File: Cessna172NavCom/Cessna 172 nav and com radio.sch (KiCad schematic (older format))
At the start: 21 parts, among them J1 Conn_02x10_Odd_Even, J2 USB_B_Micro, J6 Conn_01x05, SW1 SW_Push, SW2 SW_Push, SW3 SW_Push

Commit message: Mostly laid out
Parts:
- removed J1: Conn_02x10_Odd_Even, Connector_PinHeader_2.54mm:PinHeader_2x10_P2.54mm_Vertical, symbol Connector_Generic:Conn_02x10_Odd_Even
- removed J6: Conn_01x05, Connector_PinHeader_2.54mm:PinHeader_1x05_P2.54mm_Vertical, symbol Connector_Generic:Conn_01x05
- added C12, C13, C14, C15: 0.1uF, Capacitor_SMD:C_0805_2012Metric_Pad1.15x1.40mm_HandSolder, symbol Device:C
- added D5, D6, D7: LED, LED_THT:LED_D5.0mm, symbol Device:LED
- added J8: Conn_02x20_Odd_Even, SamacSys_Parts:SAMTEC-TST-120-01-X-D, symbol Connector_Generic:Conn_02x20_Odd_Even
- added R18, R19, R20: 220k, Resistor_SMD:R_0805_2012Metric_Pad1.15x1.40mm_HandSolder, symbol Device:R
- added SW4, SW5, SW6: SW_Push, Button_Switch_THT:SW_PUSH_6mm_H8mm, symbol Switch:SW_Push
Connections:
- net labels added: CHAN1_LED, CHAN2_LED, COMM1_KHZ_SW, COMM1_LEFT, COMM1_RIGHT, COMM1_TX_SW, COMM1_VOL_LEFT, COMM1_VOL_RIGHT, COMM2_KHZ_SW, COMM2_LEFT, COMM2_RIGHT, COMM2_TX_SW, COMM2_VOL_LEFT, COMM2_VOL_RIGHT, IDENT1_LED, IDENT1_SW, IDENT2_LED, IDENT2_SW, NAV1_KHZ_SW, NAV1_LEFT, NAV1_RIGHT, NAV1_TX_SW, NAV2_KHZ_SW, NAV2_LEFT, NAV2_RIGHT, NAV2_TX_SW, TEST1_LED, TEST1_SW, TEST2_LED, TEST2_SW
- net labels removed: CHAN_LED, COMM_KHZ_SW, COMM_LEFT, COMM_RIGHT, COMM_TX_SW, COMM_VOL_LEFT, COMM_VOL_RIGHT, DOUT, IDENT_LED, IDENT_SW, NAV_KHZ_SW, NAV_LEFT, NAV_RIGHT, NAV_TX_SW, TEST_LED, TEST_SW
- wire segments 44 -> 86
- no-connect marks 5 -> 6
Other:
- note added: "Arduino connections"
- note added: "COMM1 active"
- note added: "COMM1 standby"
- note added: "COMM1 tuning"
- note added: "COMM1 volume"
- note added: "COMM2 active"
- note added: "COMM2 standby"
- note added: "COMM2 tuning"
- note added: "COMM2 volume"
- note added: "Decoupling capacitors"
- note added: "NAV1 active"
- note added: "NAV1 standby"
- note added: "NAV1 tuning"
- note added: "NAV2 active"
- note added: "NAV2 standby"
- note added: "NAV2 tuning"
- note added: "Power"
- note added: "Test switch is on\nCOMM1 volume\nrotary encoder"
- note added: "Test switch is on\nCOMM2 volume\nrotary encoder"
- note removed: "COMM"
- note removed: "COMM active"
- note removed: "COMM standby"
- note removed: "COMM volume"
- note removed: "NAV"
- note removed: "NAV active"
- note removed: "NAV standby"
- note removed: "Power and board connection"
- note removed: "Test switch is on\nCOMM volume\nrotary encoder"
- moved on the sheet: C1, C2, C3, C4, C5, D1, D2, D3, D4, J2, R1, R17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

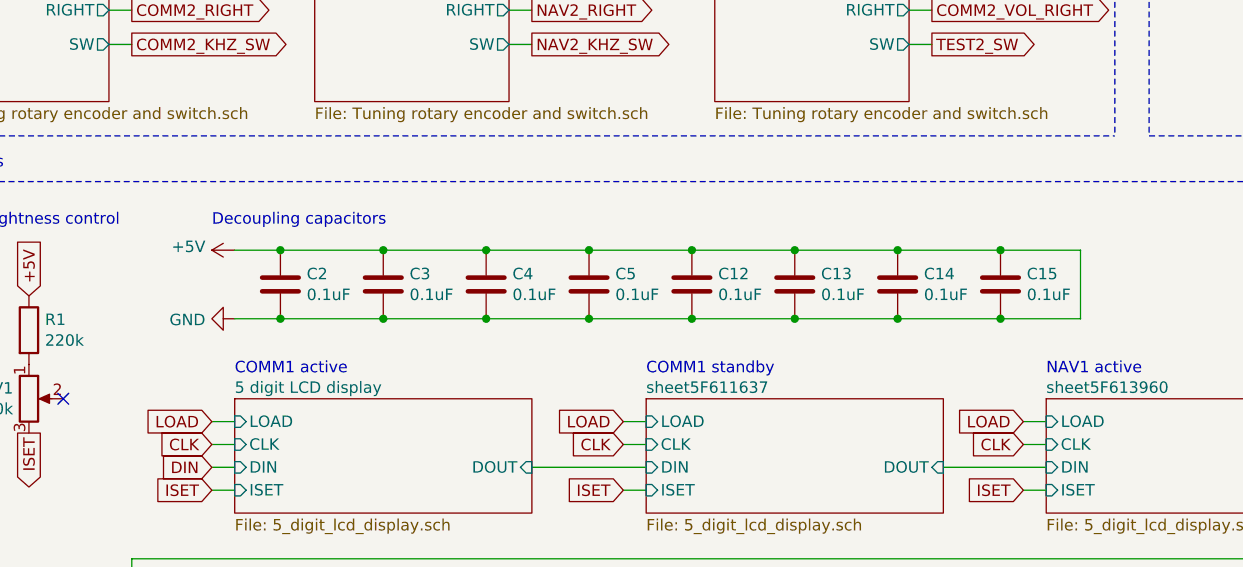
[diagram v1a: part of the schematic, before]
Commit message: Full 2up layout done
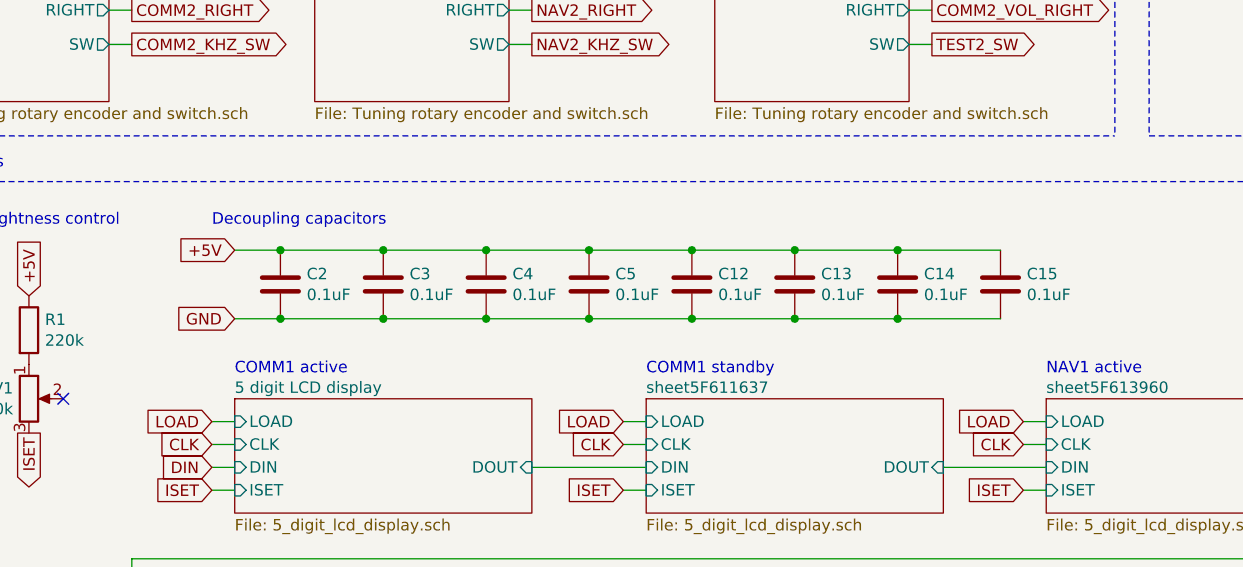
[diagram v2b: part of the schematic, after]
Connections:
- net +5V: no longer C1.2, C12.2, C13.2, C14.2, C15.2, C2.2, C3.2, C4.2, C5.2, D1.1 (K), D2.1 (K), D3.1 (K), D4.1 (K), D5.1 (K), D6.1 (K), D7.1 (K), J2.5 (GND), SW1.1, SW2.1, SW3.1, SW4.1, SW5.1, SW6.1
- new net GND: C1.2, C12.2, C13.2, C14.2, C15.2, C2.2, C3.2, C4.2, C5.2, D1.1 (K), D2.1 (K), D3.1 (K), D4.1 (K), D5.1 (K), D6.1 (K), D7.1 (K), J2.5 (GND), SW1.1, SW2.1, SW3.1, SW4.1, SW5.1, SW6.1
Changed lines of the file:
@@
 	4300 7100 4350 7100
-$Comp
-L power:+5V #PWR0101
-U 1 1 5F65C5FC
-P 2050 3500
-F 0 "#PWR0101" H 2050 3350 50  0001 C CNN
-F 1 "+5V" V 2065 3628 50  0000 L CNN
-F 2 "" H 2050 3500 50  0001 C CNN
-F 3 "" H 2050 3500 50  0001 C CNN
-	1    2050 3500
-	0    -1   -1   0
-$EndComp
-$Comp
-L power:GND #PWR0102
-U 1 1 5F65CDCA
-P 2050 3800
-F 0 "#PWR0102" H 2050 3550 50  0001 C CNN
-F 1 "GND" V 2055 3672 50  0000 R CNN
-F 2 "" H 2050 3800 50  0001 C CNN
-F 3 "" H 2050 3800 50  0001 C CNN
-	1    2050 3800
-	0    1    1    0
-$EndComp
 $Comp
 L Device:C C12
@@
 	1    0    0    -1
 $EndComp
-Connection ~ 5400 3500
-Connection ~ 5400 3800
 $Comp
 L Device:C C13
@@
 	4950 3800 5400 3800
 Connection ~ 4950 3800
-Wire Wire Line
-	5750 3500 5750 3800
-Wire Wire Line
-	5400 3800 5750 3800
-Wire Wire Line
-	5400 3500 5750 3500
 Wire Wire Line
 	3600 3500 4050 3500
@@
 Text GLabel 10250 4850 1    50   Input ~ 0
 +5V
+Text GLabel 2050 3800 0    50   Input ~ 0
+GND
+Text GLabel 2050 3500 0    50   Input ~ 0
++5V
 $EndSCHEMATC

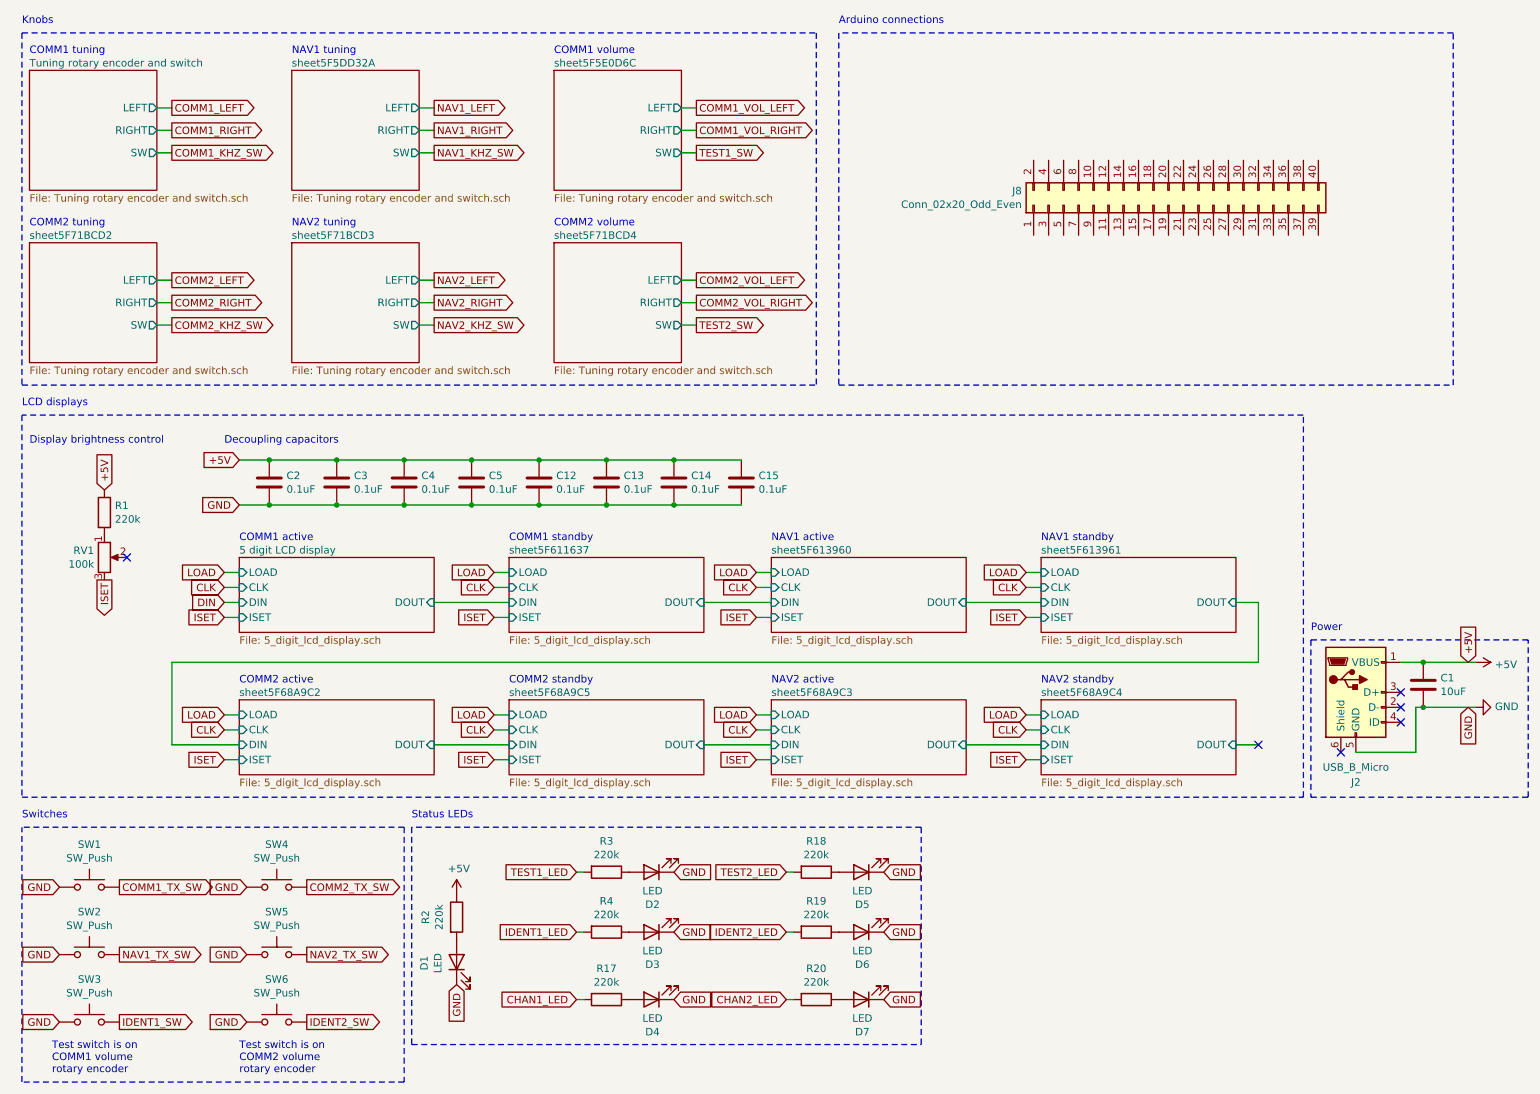
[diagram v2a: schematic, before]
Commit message: Merge connector mapping
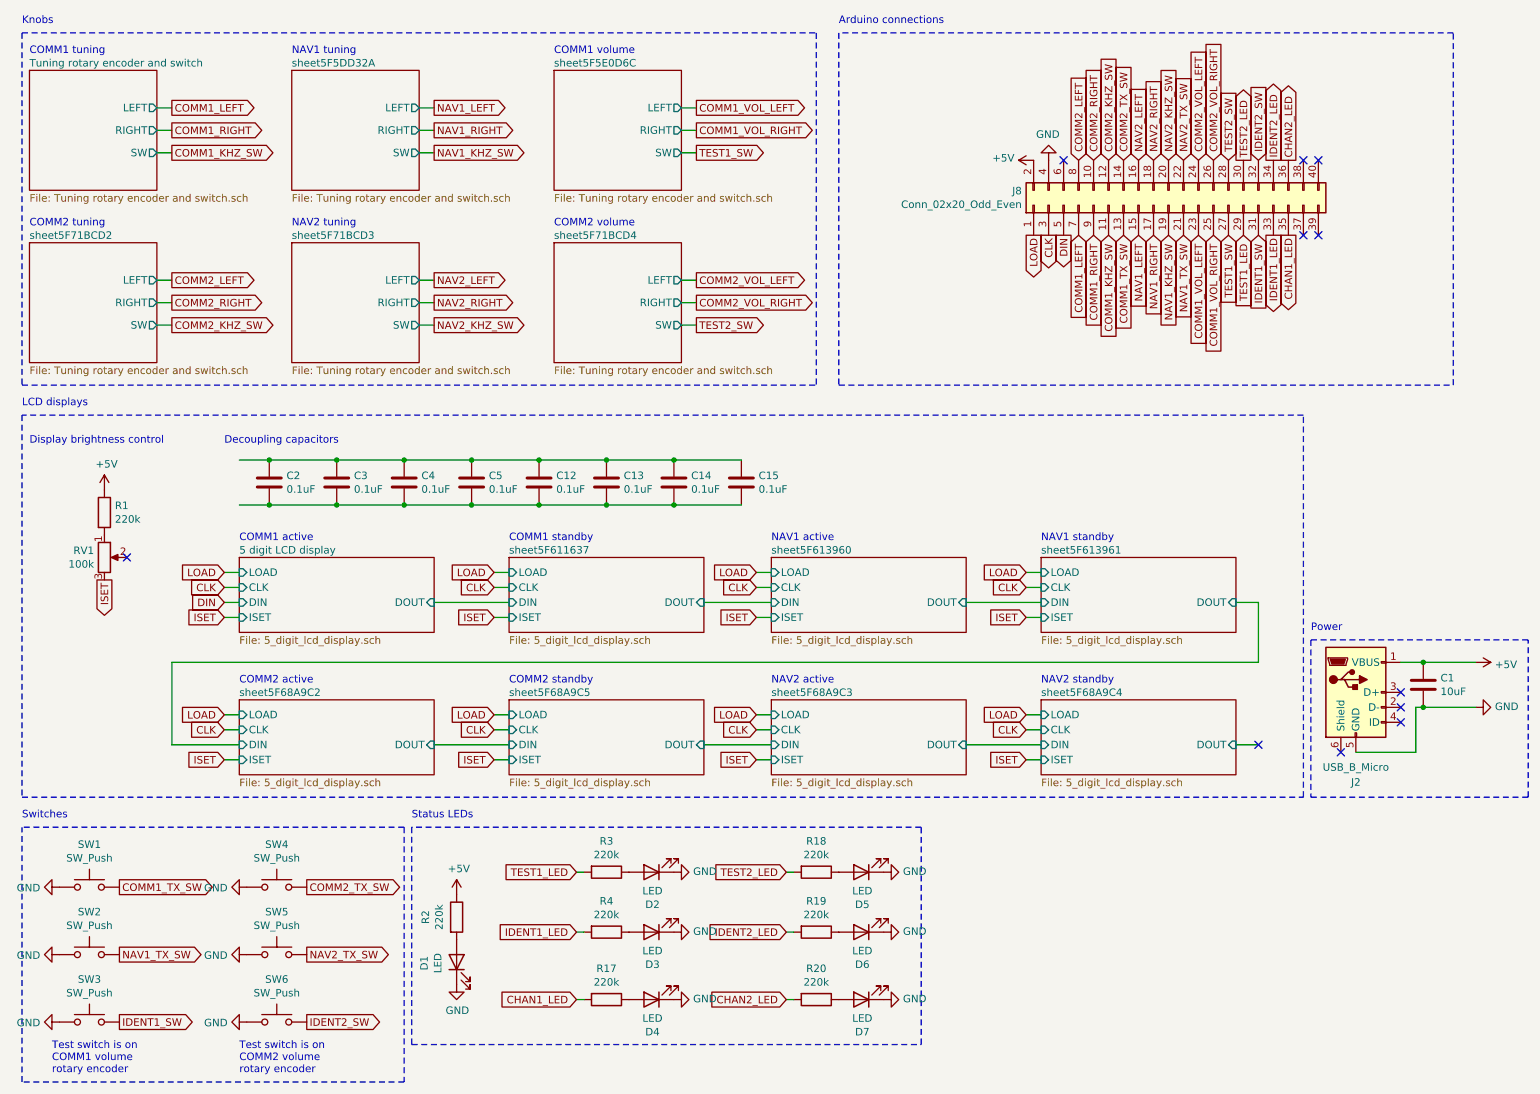
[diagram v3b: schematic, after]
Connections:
- net +5V: now also J8.2 (Pin_2); no longer C12.1, C13.1, C14.1, C15.1, C2.1, C3.1, C4.1, C5.1
- net CHAN1_LED: now also J8.35 (Pin_35)
- net CHAN2_LED: now also J8.36 (Pin_36)
- net CLK: now also J8.3 (Pin_3)
- net COMM1_KHZ_SW: now also J8.11 (Pin_11)
- net COMM1_LEFT: now also J8.7 (Pin_7)
- net COMM1_RIGHT: now also J8.9 (Pin_9)
- net COMM1_TX_SW: now also J8.13 (Pin_13)
- net COMM1_VOL_LEFT: now also J8.23 (Pin_23)
- net COMM1_VOL_RIGHT: now also J8.25 (Pin_25)
- net COMM2_KHZ_SW: now also J8.12 (Pin_12)
- net COMM2_LEFT: now also J8.8 (Pin_8)
- net COMM2_RIGHT: now also J8.10 (Pin_10)
- net COMM2_TX_SW: now also J8.14 (Pin_14)
- net COMM2_VOL_LEFT: now also J8.24 (Pin_24)
- net COMM2_VOL_RIGHT: now also J8.26 (Pin_26)
- net DIN: now also J8.5 (Pin_5)
- net GND: now also J8.4 (Pin_4); no longer C12.2, C13.2, C14.2, C15.2, C2.2, C3.2, C4.2, C5.2
- net IDENT1_LED: now also J8.33 (Pin_33)
- net IDENT1_SW: now also J8.31 (Pin_31)
- net IDENT2_LED: now also J8.34 (Pin_34)
- net IDENT2_SW: now also J8.32 (Pin_32)
- net LOAD: now also J8.1 (Pin_1)
- net NAV1_KHZ_SW: now also J8.19 (Pin_19)
- net NAV1_LEFT: now also J8.15 (Pin_15)
- net NAV1_RIGHT: now also J8.17 (Pin_17)
- net NAV1_TX_SW: now also J8.21 (Pin_21)
- net NAV2_KHZ_SW: now also J8.20 (Pin_20)
- net NAV2_LEFT: now also J8.16 (Pin_16)
- net NAV2_RIGHT: now also J8.18 (Pin_18)
- net NAV2_TX_SW: now also J8.22 (Pin_22)
- net TEST1_LED: now also J8.29 (Pin_29)
- net TEST1_SW: now also J8.27 (Pin_27)
- net TEST2_LED: now also J8.30 (Pin_30)
- net TEST2_SW: now also J8.28 (Pin_28)
- new net: C12.1, C13.1, C14.1, C15.1, C2.1, C3.1, C4.1, C5.1
- new net: C12.2, C13.2, C14.2, C15.2, C2.2, C3.2, C4.2, C5.2
- no-connect marks 6 -> 11

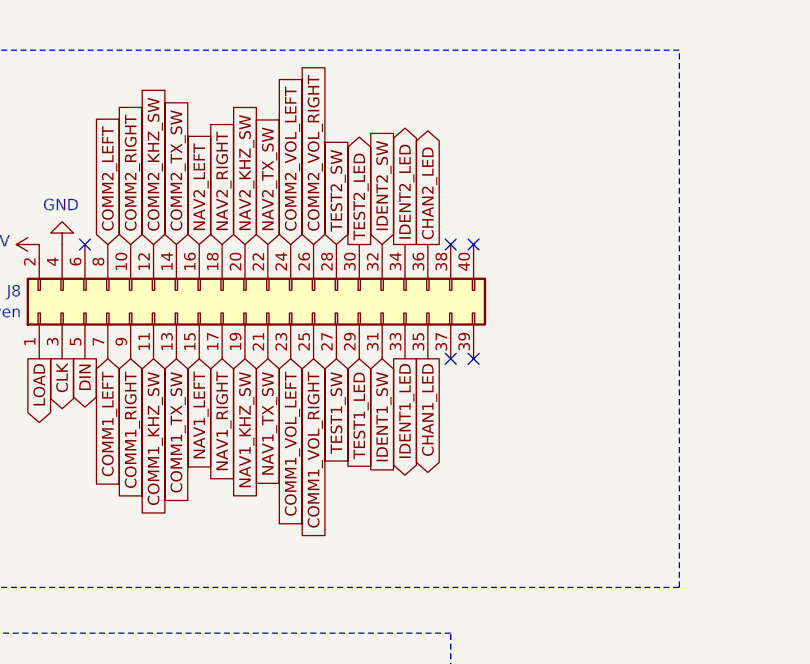
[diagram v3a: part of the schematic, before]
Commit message: Move things around to try and help router
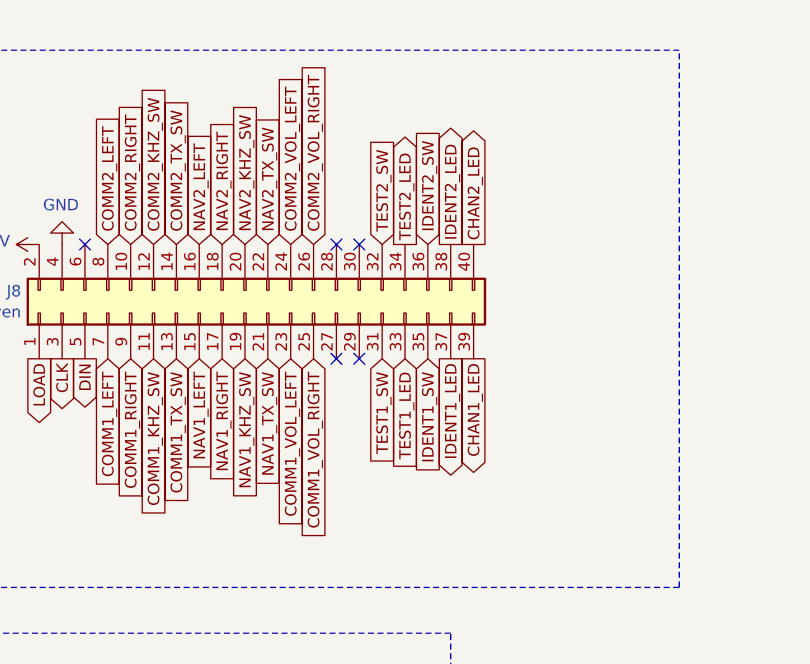
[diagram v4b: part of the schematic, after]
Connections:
- net CHAN1_LED: now also J8.39 (Pin_39); no longer J8.35 (Pin_35)
- net CHAN2_LED: now also J8.40 (Pin_40); no longer J8.36 (Pin_36)
- net IDENT1_LED: now also J8.37 (Pin_37); no longer J8.33 (Pin_33)
- net IDENT1_SW: now also J8.35 (Pin_35); no longer J8.31 (Pin_31)
- net IDENT2_LED: now also J8.38 (Pin_38); no longer J8.34 (Pin_34)
- net IDENT2_SW: now also J8.36 (Pin_36); no longer J8.32 (Pin_32)
- net TEST1_LED: now also J8.33 (Pin_33); no longer J8.29 (Pin_29)
- net TEST1_SW: now also J8.31 (Pin_31); no longer J8.27 (Pin_27)
- net TEST2_LED: now also J8.34 (Pin_34); no longer J8.30 (Pin_30)
- net TEST2_SW: now also J8.32 (Pin_32); no longer J8.28 (Pin_28)
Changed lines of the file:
@@
 Text GLabel 8550 2000 3    50   Input ~ 0
 COMM1_VOL_RIGHT
-Text GLabel 8650 2000 3    50   Input ~ 0
+Text GLabel 8850 2000 3    50   Input ~ 0
 TEST1_SW
 Text GLabel 7950 2000 3    50   Input ~ 0
@@
 Text GLabel 8350 2000 3    50   Input ~ 0
 NAV1_TX_SW
-Text GLabel 8850 2000 3    50   Input ~ 0
+Text GLabel 9050 2000 3    50   Input ~ 0
 IDENT1_SW
-Text GLabel 8750 2000 3    50   Input ~ 0
+Text GLabel 8950 2000 3    50   Input ~ 0
 TEST1_LED
-Text GLabel 8950 2000 3    50   Output ~ 0
+Text GLabel 9150 2000 3    50   Output ~ 0
 IDENT1_LED
-Text GLabel 9050 2000 3    50   Output ~ 0
+Text GLabel 9250 2000 3    50   Output ~ 0
 CHAN1_LED
 Text GLabel 7650 1500 1    50   Input ~ 0
@@
 Text GLabel 8550 1500 1    50   Input ~ 0
 COMM2_VOL_RIGHT
-Text GLabel 8650 1500 1    50   Input ~ 0
+Text GLabel 8850 1500 1    50   Input ~ 0
 TEST2_SW
-Text GLabel 8750 1500 1    50   Output ~ 0
+Text GLabel 8950 1500 1    50   Output ~ 0
 TEST2_LED
-Text GLabel 8950 1500 1    50   Output ~ 0
+Text GLabel 9150 1500 1    50   Output ~ 0
 IDENT2_LED
-Text GLabel 9050 1500 1    50   Output ~ 0
+Text GLabel 9250 1500 1    50   Output ~ 0
 CHAN2_LED
-Text GLabel 8850 1500 1    50   Input ~ 0
+Text GLabel 9050 1500 1    50   Input ~ 0
 IDENT2_SW
-NoConn ~ 9150 2000
-NoConn ~ 9250 2000
-NoConn ~ 9250 1500
-NoConn ~ 9150 1500
 NoConn ~ 7550 1500
 $Comp
@@
 	1    0    0    -1
 $EndComp
+NoConn ~ 8650 1500
+NoConn ~ 8750 1500
+NoConn ~ 8750 2000
+NoConn ~ 8650 2000
 $EndSCHEMATC

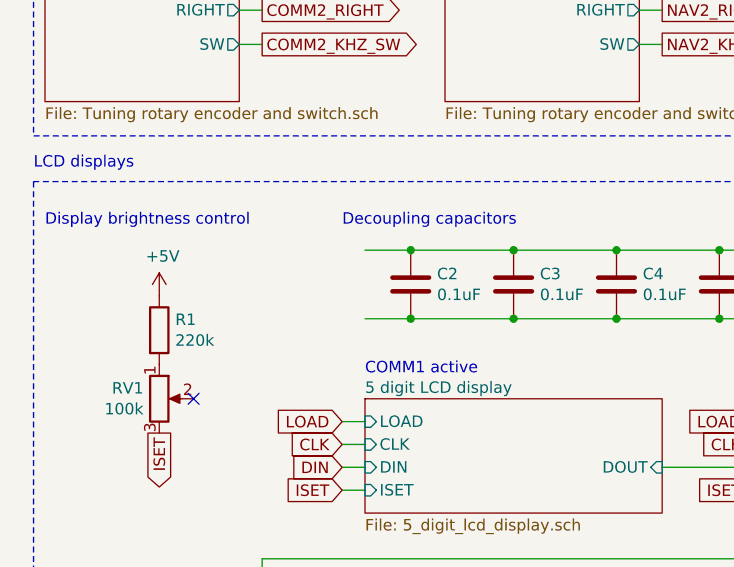
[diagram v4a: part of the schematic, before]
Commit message: Fix courtyard overlap for routing
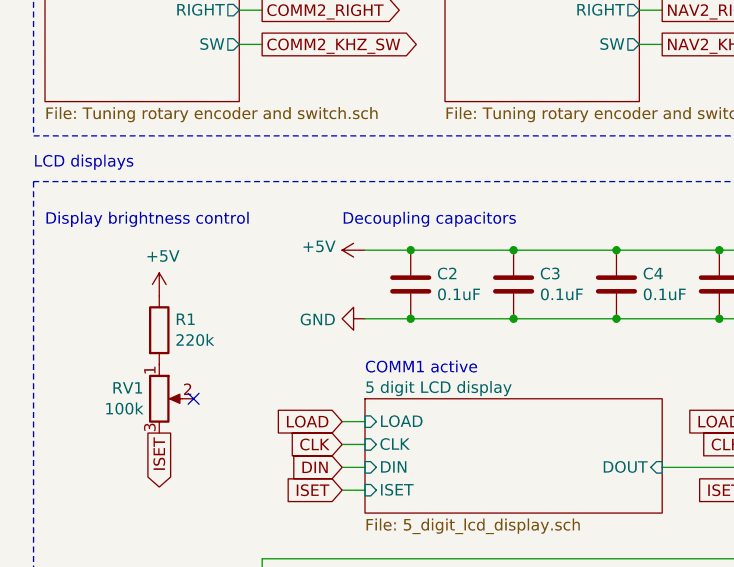
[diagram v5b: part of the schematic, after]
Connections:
- net +5V: now also C12.1, C13.1, C14.1, C15.1, C2.1, C3.1, C4.1, C5.1
- net GND: now also C12.2, C13.2, C14.2, C15.2, C2.2, C3.2, C4.2, C5.2
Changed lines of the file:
@@
 NoConn ~ 8750 2000
 NoConn ~ 8650 2000
+$Comp
+L power:+5V #PWR?
+U 1 1 5F695056
+P 2050 3500
+F 0 "#PWR?" H 2050 3350 50  0001 C CNN
+F 1 "+5V" V 2065 3628 50  0000 L CNN
+F 2 "" H 2050 3500 50  0001 C CNN
+F 3 "" H 2050 3500 50  0001 C CNN
+	1    2050 3500
+	0    -1   -1   0
+$EndComp
+$Comp
+L power:GND #PWR?
+U 1 1 5F6951C0
+P 2050 3800
+F 0 "#PWR?" H 2050 3550 50  0001 C CNN
+F 1 "GND" V 2055 3672 50  0000 R CNN
+F 2 "" H 2050 3800 50  0001 C CNN
+F 3 "" H 2050 3800 50  0001 C CNN
+	1    2050 3800
+	0    1    1    0
+$EndComp
 $EndSCHEMATC
